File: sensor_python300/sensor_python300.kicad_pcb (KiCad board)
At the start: 4 copper layers, 30 x 30 mm, 76 parts, among them J101 DF40HC(4.0)-60DS-0.4V(51), U101 NOIP1SN0300A-QTI, U102 TPS7A2033PDBVR, U103 TPS22918DBVR, U104 TPS7A2033PDBVR, U105 APX803S, U106 TPS610995DRVR, X101 <DNP> DSC1103DI5-360.0000

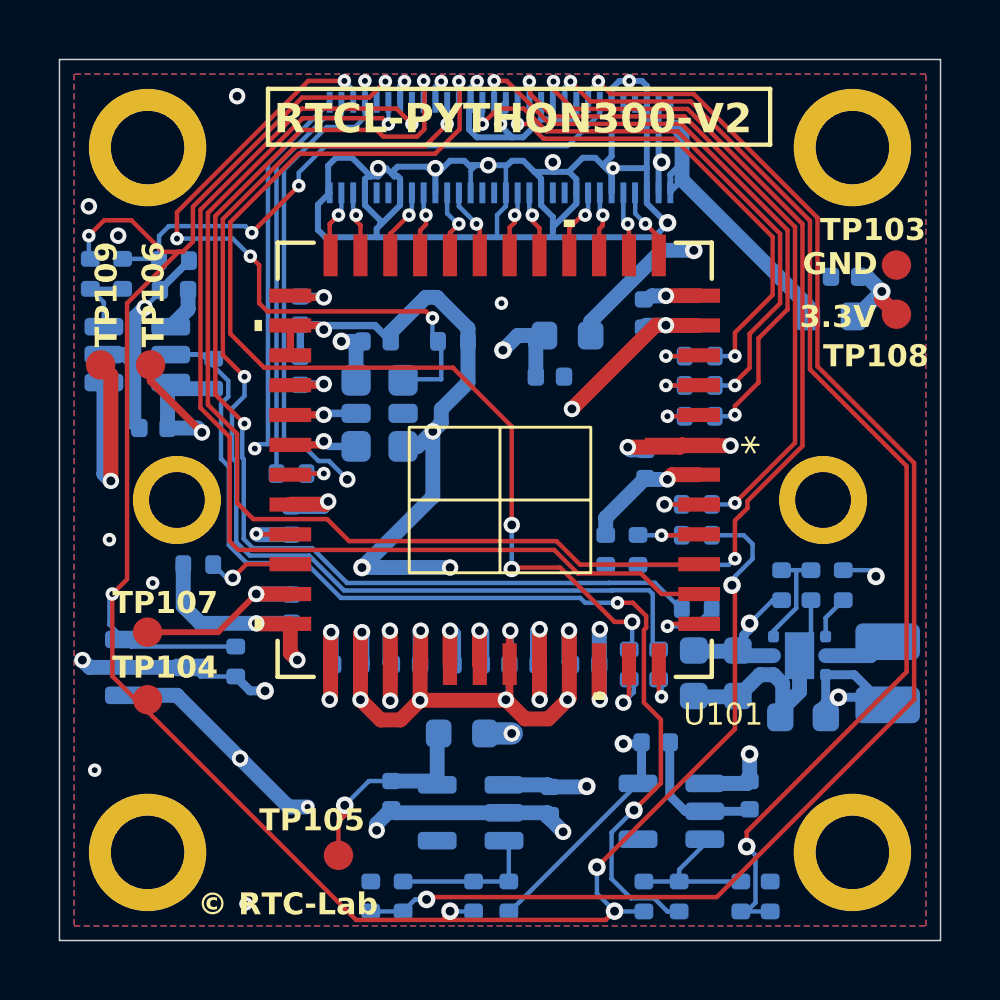
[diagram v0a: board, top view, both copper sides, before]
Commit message: Update KiCad project files for sensor_python300
- Changed active layer from 0 to 2 in sensor_python300.kicad_prl.
- Modified selection filter settings to disable dimensions, footprints, graphics, keepouts, other items, pads, text, and zones.
- Updated visible layers in sensor_python300.kicad_prl for better layer management.
- Adjusted design rules in sensor_python300.kicad_pro:
  - Reduced minimum copper edge clearance from 0.5 to 0.2.
  - Increased minimum hole clearance from 0.25 to 0.28 and minimum hole-to-hole distance from 0.25 to 0.45.
  - Decreased minimum text height from 0.75 to 0.1 and thickness from 0.15 to 0.01.
  - Updated minimum through hole diameter from 0.2 to 0.3.
  - Reduced minimum via annular width from 0.1 to 0.05 and diameter from 0.46 to 0.4.
- Changed track width from 0.1016 to 0.156464 and via diameter from 0.6 to 0.45.
- Updated via drill size from 0.2 to 0.3 for improved manufacturability.
- Added new netclass pattern for "Default" netclass matching "DOUT*".
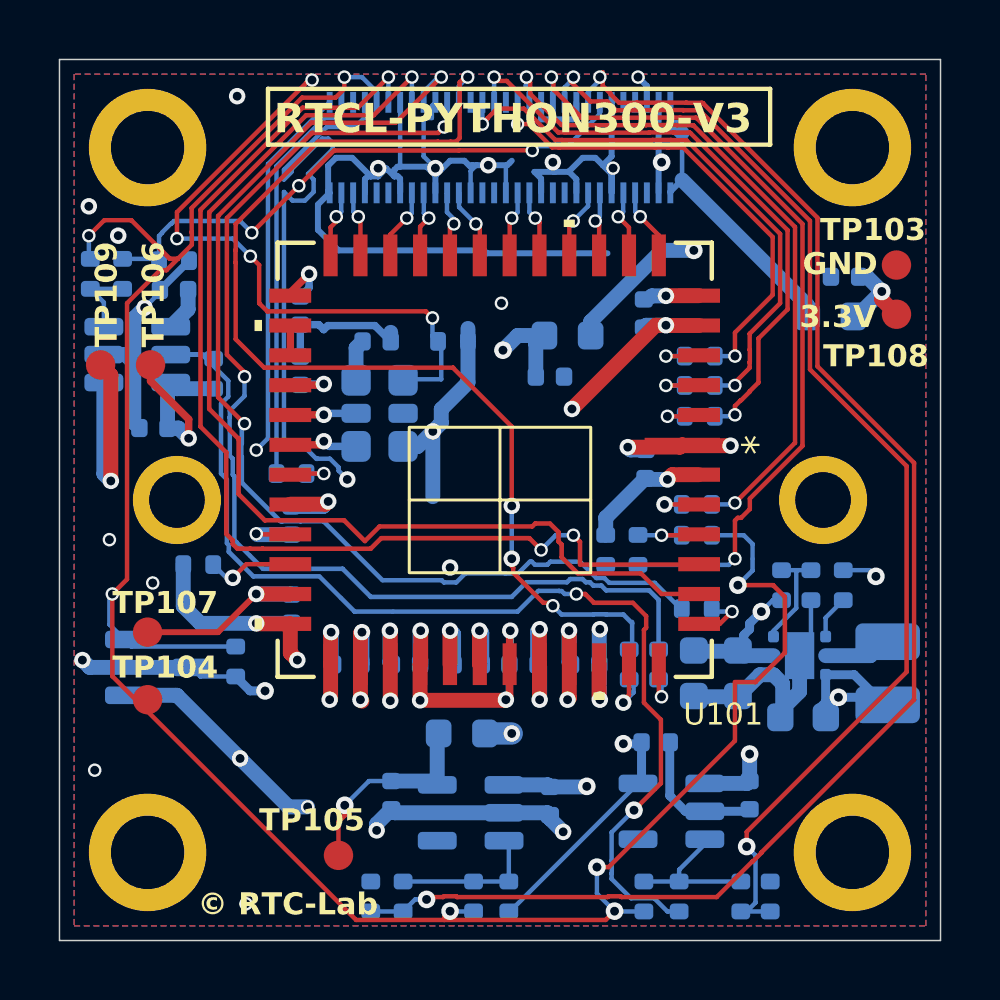
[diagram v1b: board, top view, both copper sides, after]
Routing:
- net GND: track 371.5 -> 314.7 mm, vias 46 -> 38
- net /MONITOR1: track 35.2 -> 38.3 mm, vias 1 -> 3
- net /PGOOD: track 76.2 -> 78.7 mm
- net /OSC_EN: track 23.4 -> 21.6 mm
- net /CON_V33: track 11.0 -> 9.83 mm
- net Net-(U101-trigger2): track 2.87 -> 2.02 mm
- net VDD_33: track 83.0 -> 82.2 mm, vias 7 -> 6
- net /PGOOD_VDD18: track 37.5 -> 38.3 mm
- net /PWR_EN_PIX: track 49.5 -> 50.2 mm
- net VDD_18: track 36.9 -> 37.5 mm
- net /TRIGGER1: track 38.2 -> 38.8 mm
- net +3V6: track 21.0 -> 21.5 mm
- net /TRIGGER0: track 36.9 -> 37.4 mm
- net /PWR_EN_VDD18: track 19.8 -> 19.7 mm, vias 2 -> 3
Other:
- board text added: "RTCL-PYTHON300-V3"
- board text removed: "RTCL-PYTHON300-V2"

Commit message: Update schematic and project settings for sensor_python300
- Modified selection filter in project settings to enable footprint and text visibility.
- Updated visible layers configuration for better layer management.
- Added new junctions and wires in the schematic to improve connectivity.
- Introduced a new capacitor (C130) with appropriate properties and connections.
- Replaced the existing GND symbol with a new instance for better clarity and organization.
- Adjusted positions of several components for improved layout and readability.
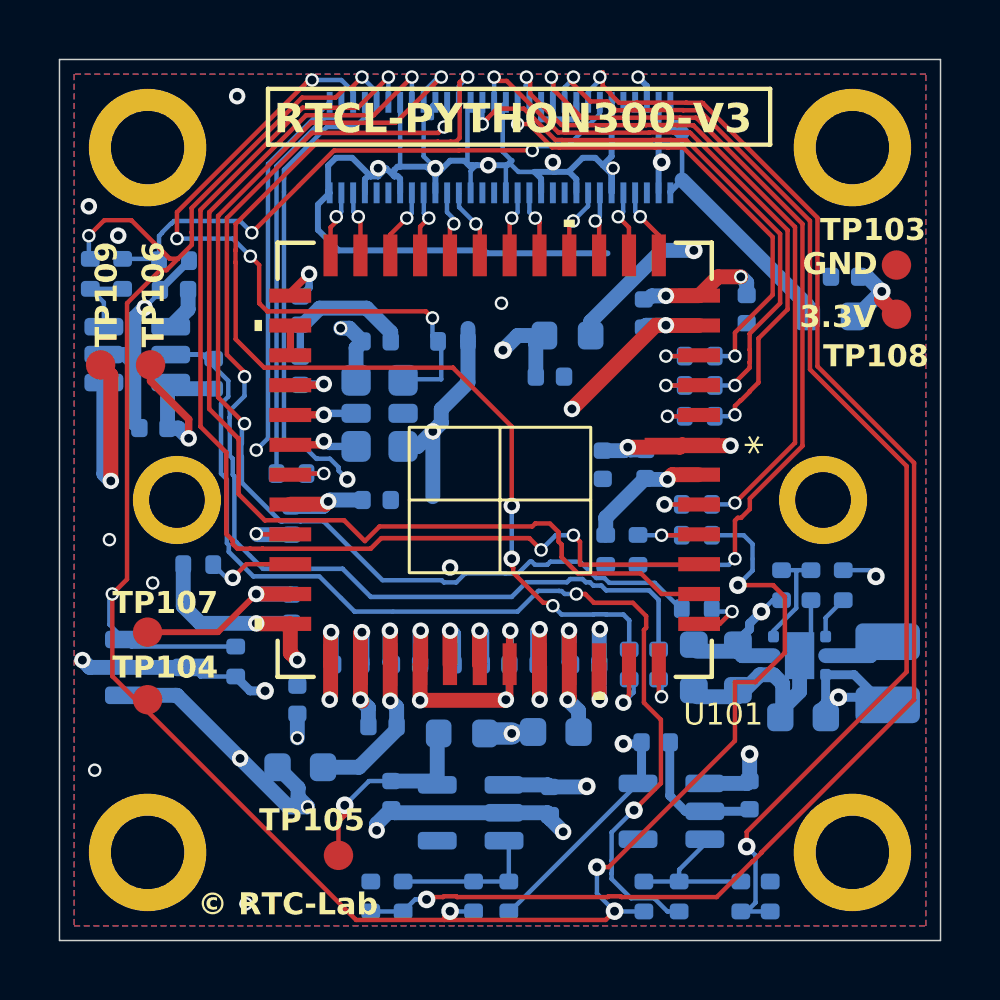
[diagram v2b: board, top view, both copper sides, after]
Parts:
- added C115: 4.7uF, Capacitor_SMD:C_0402_1005Metric, B.Cu at (146.0, 107.7)
- added C125: 10uF, Capacitor_SMD:C_0603_1608Metric, B.Cu at (151.9, 107.9)
- added C126: 4.7uF, Capacitor_SMD:C_0402_1005Metric, B.Cu at (143.1, 106.8)
- added C127: 4.7uF, Capacitor_SMD:C_0402_1005Metric, B.Cu at (145.8, 100.0)
- added C128: 4.7uF, Capacitor_SMD:C_0402_1005Metric, B.Cu at (153.5, 98.8)
- added C129: 4.7uF, Capacitor_SMD:C_0402_1005Metric, B.Cu at (158.4, 93.5)
- added C130: 10uF, Capacitor_SMD:C_0603_1608Metric, B.Cu at (143.2, 109.1)
- C116, C117: value 1uF -> 10uF
- C118: value 4.7uF -> 10uF
- U105: value APX803S -> APX803S-29SA-7
- moved C123 0.20 mm to (156.6, 105.7)
- moved C124 0.20 mm to (158.1, 105.7)
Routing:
- net VDD_33: track 82.2 -> 90.0 mm, vias 6 -> 8
- net VDD_PIX: track 52.7 -> 57.6 mm
- net VDD_18: track 37.5 -> 41.1 mm, vias 4 -> 5
- net /OSC_EN: track 21.6 -> 23.5 mm
- net GND: track 314.7 -> 313.8 mm
- net /PWR_EN_VDD18: vias 3 -> 2
